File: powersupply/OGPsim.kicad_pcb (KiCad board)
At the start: 2 copper layers, 35.8 x 15.7 mm, 39 parts, among them J1 Conn_01x03, J2 Conn_01x03, J3 Conn_01x02, J4 Conn_01x02, J5 Conn_01x02, J6 Conn_01x02, J7 Conn_01x02, Q1 Q_NPN_BEC, Q2 Q_NPN_BEC, Q5 Q_NPN_BEC, U1 LM317_TO39

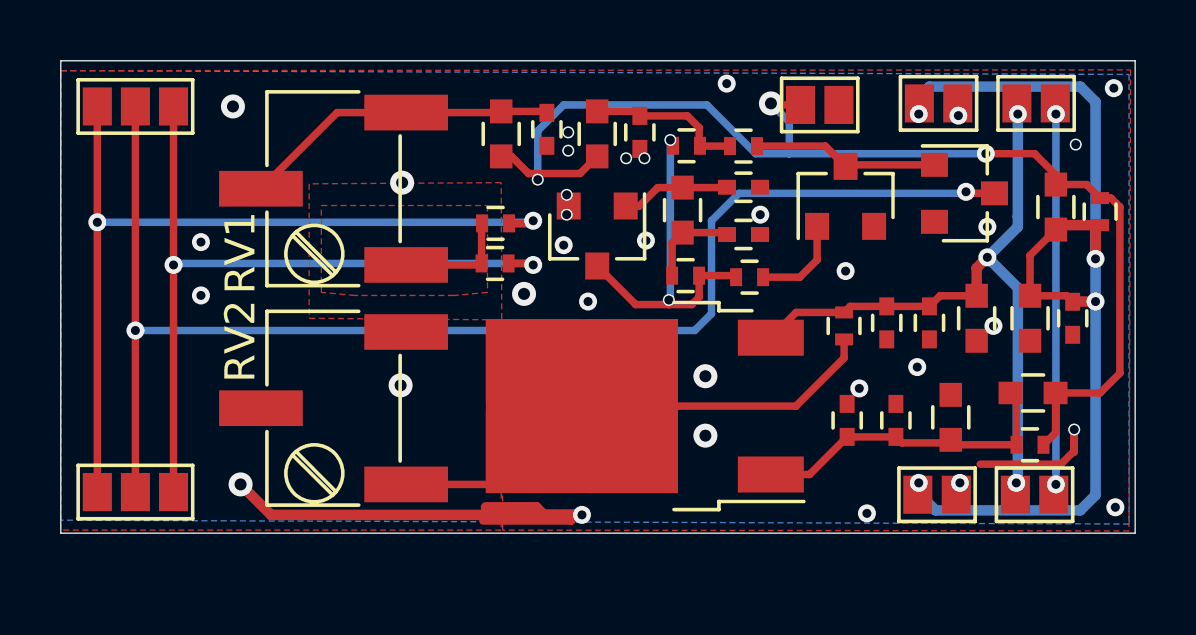
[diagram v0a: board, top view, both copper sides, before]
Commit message: Added name and date to silkscreen on all boards. Sending design to PCB fab house tonight!
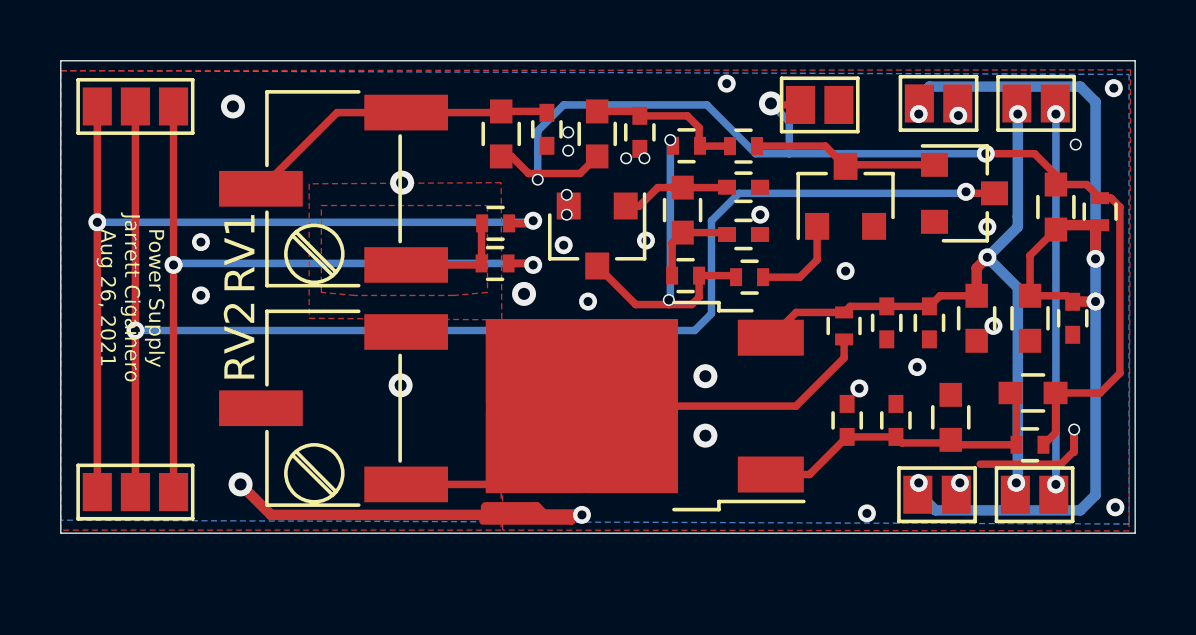
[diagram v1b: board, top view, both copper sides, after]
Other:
- board text added: "Power Supply Jarrett Cigainero Aug 26, 2021"

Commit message: Fixed LM317 having wrong pinout in schematic and on board layout.
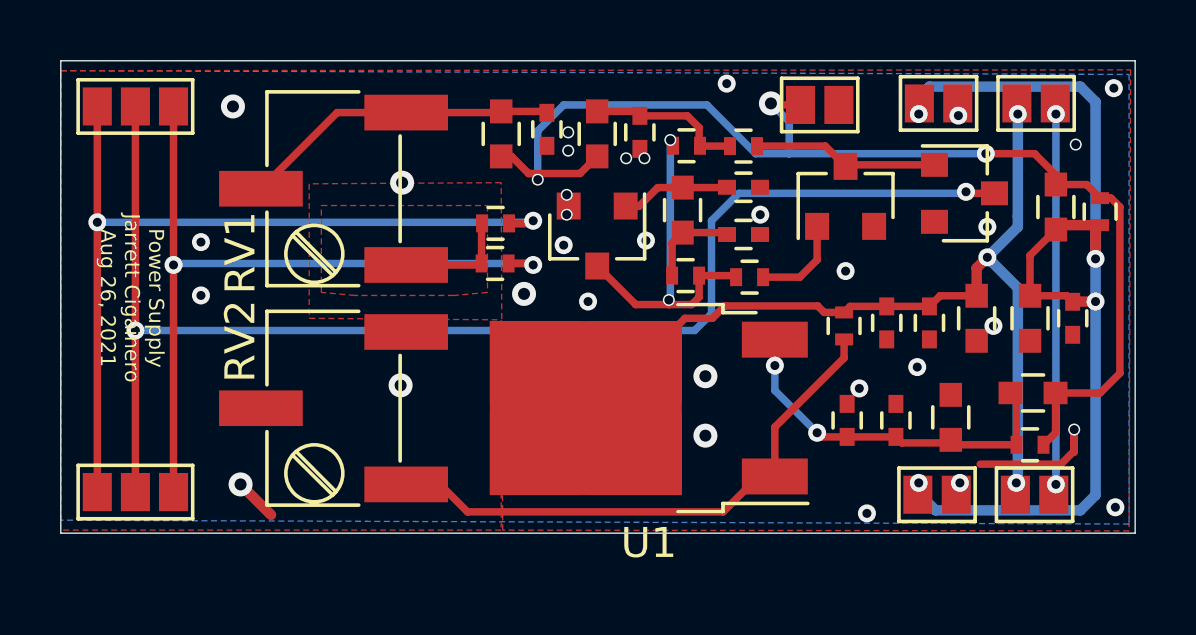
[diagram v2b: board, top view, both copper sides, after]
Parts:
- U1: value LM317_TO39 -> LM317L_SOT-89
- moved U1 0.15 mm to (151.3, 97.9)
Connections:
- U1 pad 1: Net-(C7-Pad2) -> Net-(R7-Pad1)
- U1 pad 2: Net-(R7-Pad1) -> +4V
- U1 pad 3: +4V -> Net-(C7-Pad2)
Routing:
- net GND: track 23.3 -> 6.23 mm, vias 33 -> 32
- net +4V: track 22.0 -> 33.0 mm
- net Net-(R7-Pad1): track 17.0 -> 19.5 mm
- net Net-(C7-Pad2): track 10.6 -> 12.3 mm, vias 0 -> 2
